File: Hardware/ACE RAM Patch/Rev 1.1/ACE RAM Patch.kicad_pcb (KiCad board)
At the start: 2 copper layers, 46 x 22 mm, 4 parts, among them J1 74HC00 (U13), U1 74HC00, U2 74HC02

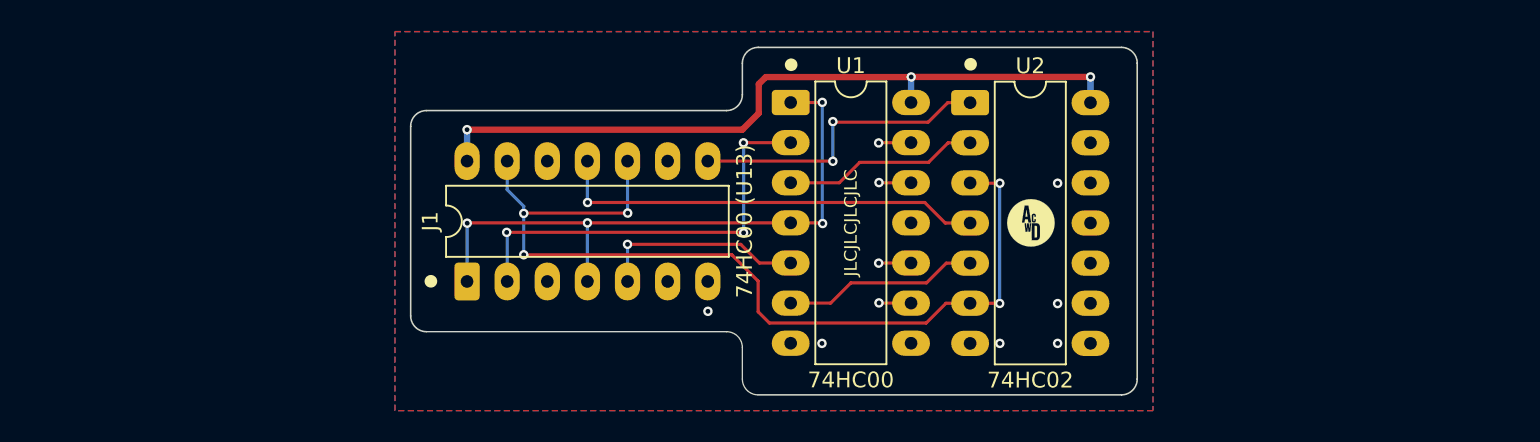
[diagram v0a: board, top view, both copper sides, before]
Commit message: ACE RAM Patch Rev 1.1: lay it out to mount under the ACE
U12 and U13 come off the Rev 1.0 board, chips and sockets, and the patch is
soldered underneath on pin headers, front side up. U1, J1, J2 and U2 sit in
one row, 92.6 x 13.1 mm: J1 and J2 on the front, into U12's and U13's holes,
and U1 and U2 on the back, hanging below. J2 is 23.00 mm from J1, and all 28
header pins land on U12's and U13's pads on the Rev 1.0 board to 0.0000 mm.

No DRC errors, nothing unconnected, no schematic parity issues, and power
flags clear the schematic's ERC. Production files are generated as Rev 1.1,
and their gerbers and drill files match the board shape for shape.

Co-Authored-By: Claude Opus 5.5 (1M context) <noreply@anthropic.com>
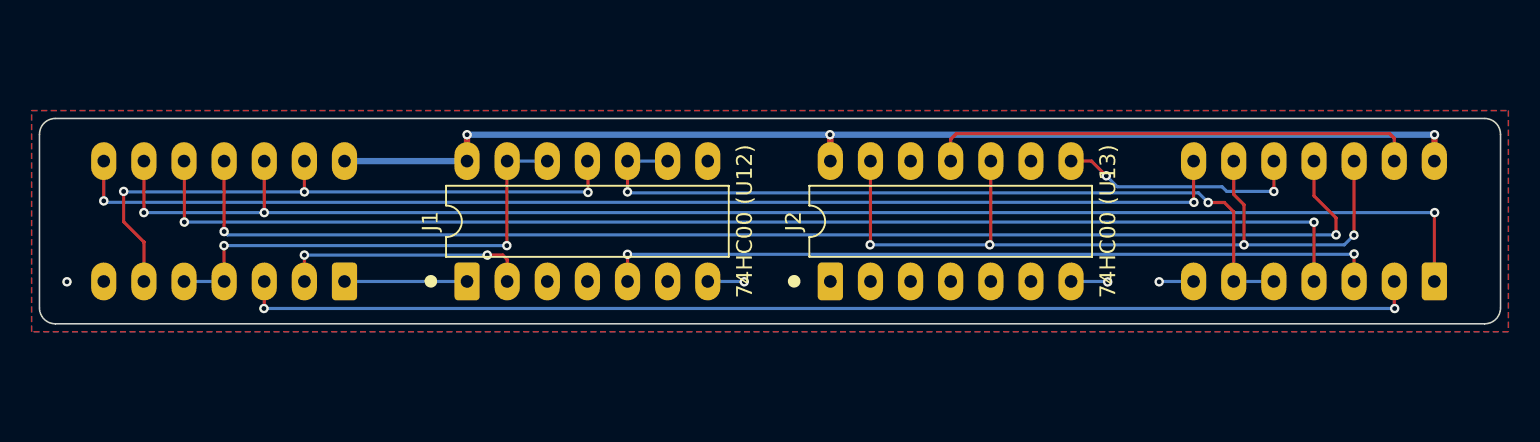
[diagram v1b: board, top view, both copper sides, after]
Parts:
- removed G***: LOGO, A.C. Wright Design Logo:A.C. Wright Logo 3mm
- added J2: 74HC00 (U13), Package_DIP:DIP-14_W7.62mm_LongPads, F.Cu at (129.6, 94.8)
- J1: value 74HC00 (U13) -> 74HC00 (U12)
- U1, U2: moved to B.Cu
- moved U2 31.5 mm to (167.8, 94.8), turned to 90 degrees
- moved U1 30.4 mm to (98.8, 94.8), turned to 90 degrees
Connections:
- net U12C_PIN8 renamed A8
- J1 pad 1: U12B_PIN6 -> A9
- J1 pad 10: WB -> IO1B
- J1 pad 11: LOADH -> B18
- J1 pad 12: unconnected-(J1-Pin_12-Pad12) -> IO2B
- J1 pad 13: WB -> IO2B
- J1 pad 4: U12B_PIN6 -> unconnected-(J1-Pin_4-Pad4)
- J1 pad 5: U12D_PIN11 -> U17_PIN8
- J1 pad 8: LOADL -> unconnected-(J1-Pin_8-Pad8)
- J1 pad 9: unconnected-(J1-Pin_9-Pad9) -> IO1B
- U1 pad 1: U12B_PIN6 -> A9
- U1 pad 10: GND -> IO1
- U1 pad 11: unconnected-(U1-Pad11) -> Net-(U1-Pad11)
- U1 pad 12: GND -> BANK_SEL
- U1 pad 13: GND -> B18
- U1 pad 4: U12B_PIN6 -> IO2B
- U1 pad 5: U12D_PIN11 -> IO2B
- U1 pad 6: Net-(U1-Pad6) -> B18
- U1 pad 8: unconnected-(U1-Pad8) -> Net-(U1-Pad8)
- U1 pad 9: GND -> BANK_SEL
- U2 pad 1: LOADL -> BANK_SEL
- U2 pad 10: unconnected-(U2-Pad10) -> LOADL
- U2 pad 11: GND -> Net-(U1-Pad11)
- U2 pad 12: GND -> WB
- U2 pad 13: unconnected-(U2-Pad13) -> LOADH
- U2 pad 3: WB -> U17_PIN8
- U2 pad 4: LOADH -> IO1
- U2 pad 5: Net-(U1-Pad6) -> IO1B
- U2 pad 6: WB -> IO1B
- U2 pad 8: GND -> Net-(U1-Pad8)
- U2 pad 9: GND -> WB
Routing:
- net BANK_SEL: track 0.00 -> 92.6 mm, vias 0 -> 3
- net Net-(U1-Pad11): track 0.00 -> 80.2 mm, vias 0 -> 2
- net IO1: track 0.00 -> 79.1 mm, vias 0 -> 2
- net Net-(U1-Pad8): track 0.00 -> 74.2 mm, vias 0 -> 2
- net Net-(U1-Pad3): track 12.4 -> 75.0 mm, vias 0 -> 2
- net IO1B: track 0.00 -> 50.3 mm, vias 0 -> 2
- net U17_PIN8: track 0.00 -> 49.5 mm, vias 0 -> 2
- net U12B_PIN6: track 39.6 -> 0.00 mm, vias 4 -> 0
- net B18: track 0.00 -> 39.6 mm, vias 0 -> 3
- net IO2B: track 0.00 -> 30.6 mm, vias 0 -> 2
- net VCC: track 47.2 -> 74.0 mm
- net U12D_PIN11: track 13.2 -> 0.00 mm, vias 1 -> 0
- net Net-(U1-Pad6): track 12.4 -> 0.00 mm
- net A8: track 26.8 -> 16.0 mm, vias 3 -> 2
- net A9: track 0.00 -> 7.76 mm
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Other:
- board size 46 x 22 mm -> 92.5 x 13 mm
- board text added: "ACE RAM Patch A.C. Wright Design | Rev 1.1"
- board text removed: "ACE RAM Patch A.C. Wright Design | Rev 1.0"
- board text removed: "JLCJLCJLCJLC"
